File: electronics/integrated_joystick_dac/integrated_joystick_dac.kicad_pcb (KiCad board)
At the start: 2 copper layers, 76.2 x 55.9 mm, 15 parts, among them J1 Power/Signal Out, U1 raspberry_pi_pico, U2 MCP4728

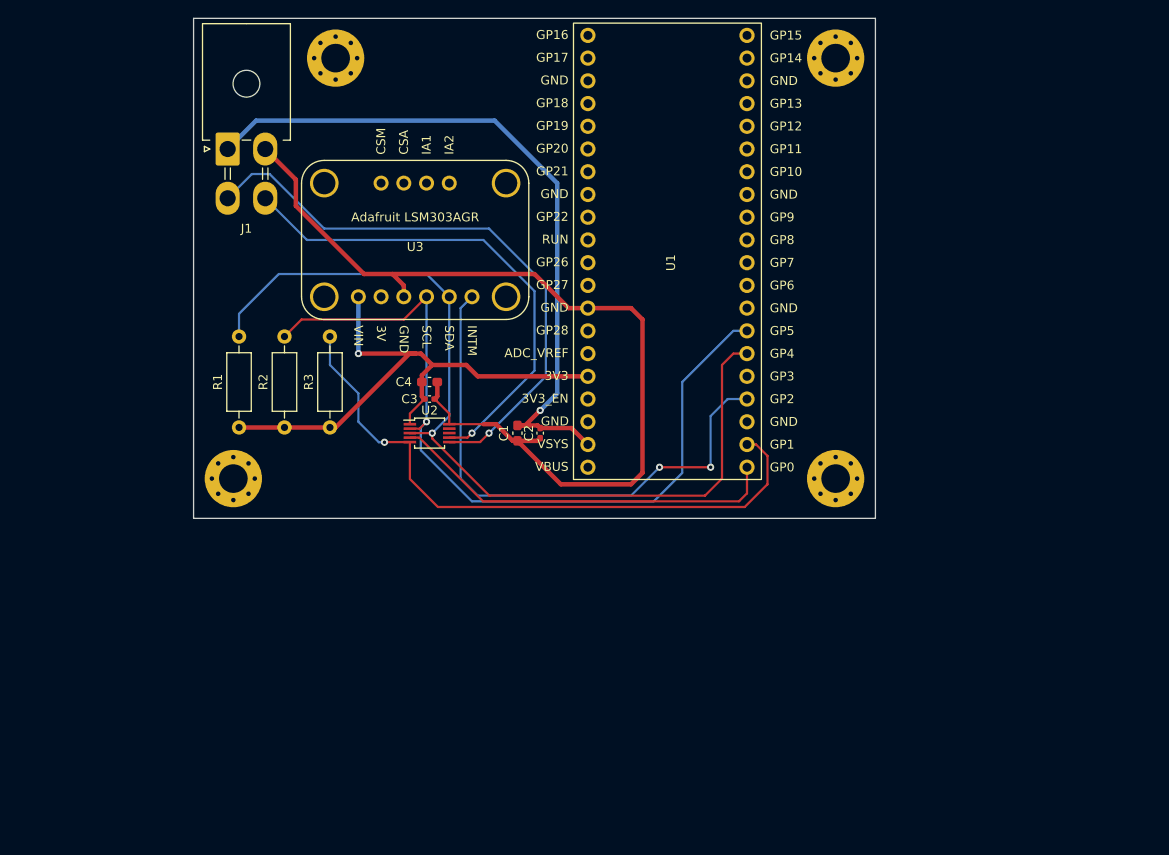
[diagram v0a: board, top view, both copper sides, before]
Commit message: start redoing board since it's too big
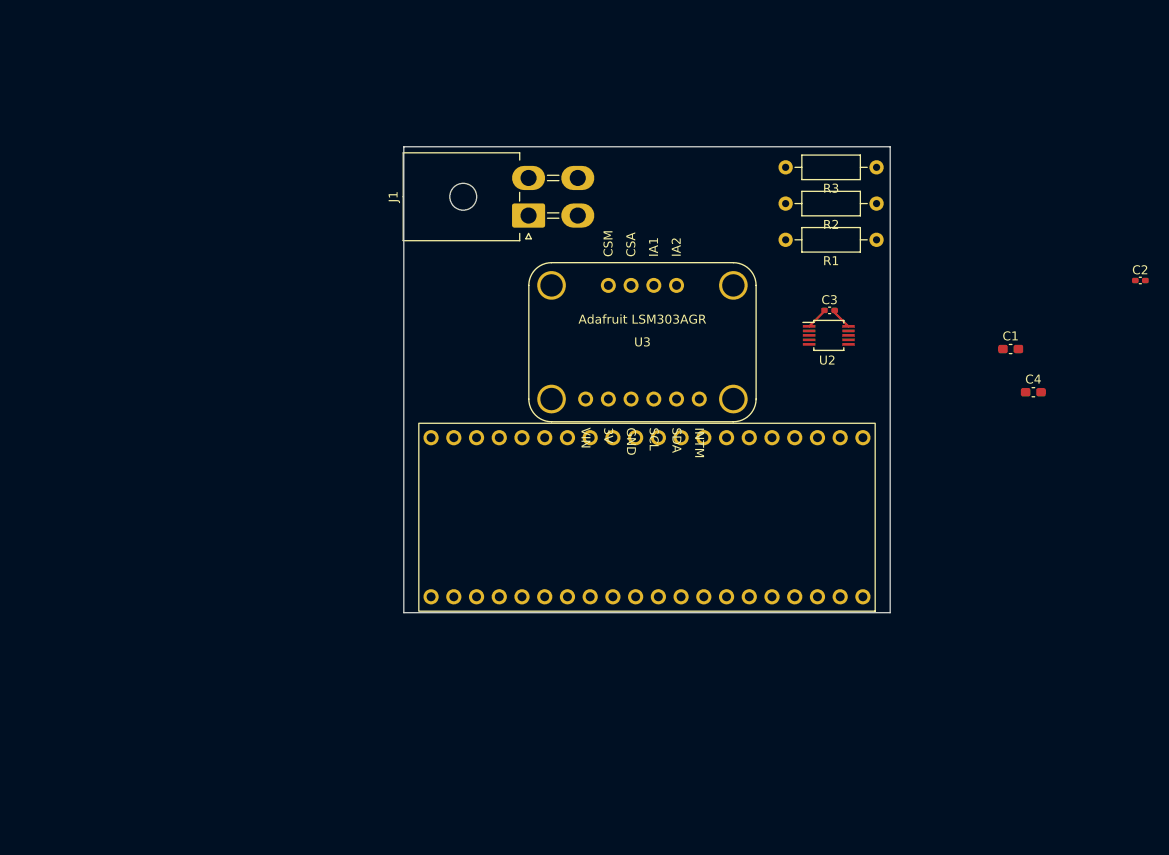
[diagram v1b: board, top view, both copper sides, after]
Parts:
- removed REF** (x4): MountingHole_3.2mm_M3_Pad_Via, MountingHole:MountingHole_3.2mm_M3_Pad_Via
- moved R1 74.3 mm to (206.5, 62.2), turned to 180 degrees
- moved R2 70.7 mm to (206.5, 58.2), turned to 180 degrees
- moved C2 69.2 mm to (236.0, 66.8), turned to 0 degrees
- moved R3 67.7 mm to (206.5, 54.1), turned to 180 degrees
- moved C4 67.5 mm to (224.0, 79.2)
- moved C1 55.9 mm to (221.5, 74.4), turned to 0 degrees
- moved U2 45.9 mm to (201.2, 72.9)
- moved C3 45.8 mm to (201.3, 70.1)
- moved J1 34.4 mm to (167.6, 59.5), turned to 90 degrees
- moved U1 28.2 mm to (182.1, 92.8), turned to 180 degrees
- moved U3 27.4 mm to (180.3, 73.7)
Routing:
- net GND: track 105.0 -> 2.43 mm
- net /SDA: track 99.9 -> 0.00 mm, vias 1 -> 0
- net /SCL: track 90.0 -> 0.00 mm, vias 1 -> 0
- net /+3V3: track 79.2 -> 0.00 mm, vias 1 -> 0
- net /RDY: track 70.0 -> 0.00 mm, vias 1 -> 0
- net /JoystickX: track 65.8 -> 0.00 mm, vias 1 -> 0
- net /+3V3_2: track 64.1 -> 2.51 mm, vias 1 -> 0
- net /INTM: track 61.5 -> 0.00 mm, vias 2 -> 0
- net /JoystickY: track 55.9 -> 0.00 mm, vias 1 -> 0
- net /LDAC: track 43.9 -> 0.00 mm
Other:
- board size 76.2 x 55.9 mm -> 54.4 x 52.1 mm

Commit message: make smaller board...
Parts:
- added REF**: MountingHole_2.7mm_M2.5_ISO7380_Pad, MountingHole:MountingHole_2.7mm_M2.5_ISO7380_Pad, F.Cu at (197.4, 78.5)
- added REF**: MountingHole_2.7mm_M2.5_ISO7380_Pad, MountingHole:MountingHole_2.7mm_M2.5_ISO7380_Pad, F.Cu at (159.3, 77.2)
- added REF**: MountingHole_2.7mm_M2.5_ISO7380_Pad, MountingHole:MountingHole_2.7mm_M2.5_ISO7380_Pad, F.Cu at (191.0, 55.6)
- moved C1 55.6 mm to (166.9, 63.8)
- moved C2 48.0 mm to (200.9, 99.6), turned to 180 degrees
- moved C4 33.5 mm to (197.4, 99.6)
- moved R1 1.62 mm to (206.0, 63.8)
- moved J1 1.30 mm to (168.9, 59.4)
- moved R2 0.92 mm to (206.0, 58.9)
- moved R3 0.51 mm to (206.0, 54.1)
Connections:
- U1 pad 13: unconnected-(U1-GND-Pad13) -> GND
- U1 pad 18: unconnected-(U1-GND-Pad18) -> GND
- U1 pad 23: unconnected-(U1-GND-Pad23) -> GND
- U1 pad 28: unconnected-(U1-GND-Pad28) -> GND
- U1 pad 3: unconnected-(U1-GND-Pad3) -> GND
- U1 pad 38: unconnected-(U1-GND-Pad38) -> GND
- U1 pad 8: unconnected-(U1-GND-Pad8) -> GND
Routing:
- net GND: track 2.43 -> 175.8 mm, vias 0 -> 1
- net /+3V3: track 0.00 -> 97.8 mm
- net /+3V3_2: track 2.51 -> 93.8 mm
- net /SCL: track 0.00 -> 73.3 mm
- net /SDA: track 0.00 -> 55.4 mm, vias 0 -> 1
- net /RDY: track 0.00 -> 47.2 mm
- net /JoystickY: track 0.00 -> 36.8 mm, vias 0 -> 1
- net /JoystickX: track 0.00 -> 34.9 mm, vias 0 -> 1
- net /INTM: track 0.00 -> 15.3 mm
- net /LDAC: track 0.00 -> 14.0 mm
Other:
- board size 54.4 x 52.1 mm -> 53.3 x 52.1 mm
- board text added: "SCTS Engineering Umptysquatch X Joystick DAC Board"

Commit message: move connector back (probably too far)
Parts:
- removed the REF** at (191.0, 55.6)
- moved C1 20.1 mm to (186.9, 63.5)
- moved J1 17.3 mm to (186.2, 59.4)
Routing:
- net /+3V3: track 97.8 -> 114.9 mm
- net /JoystickX: track 34.9 -> 20.2 mm
- net /JoystickY: track 36.8 -> 23.6 mm
- net GND: track 175.8 -> 179.8 mm

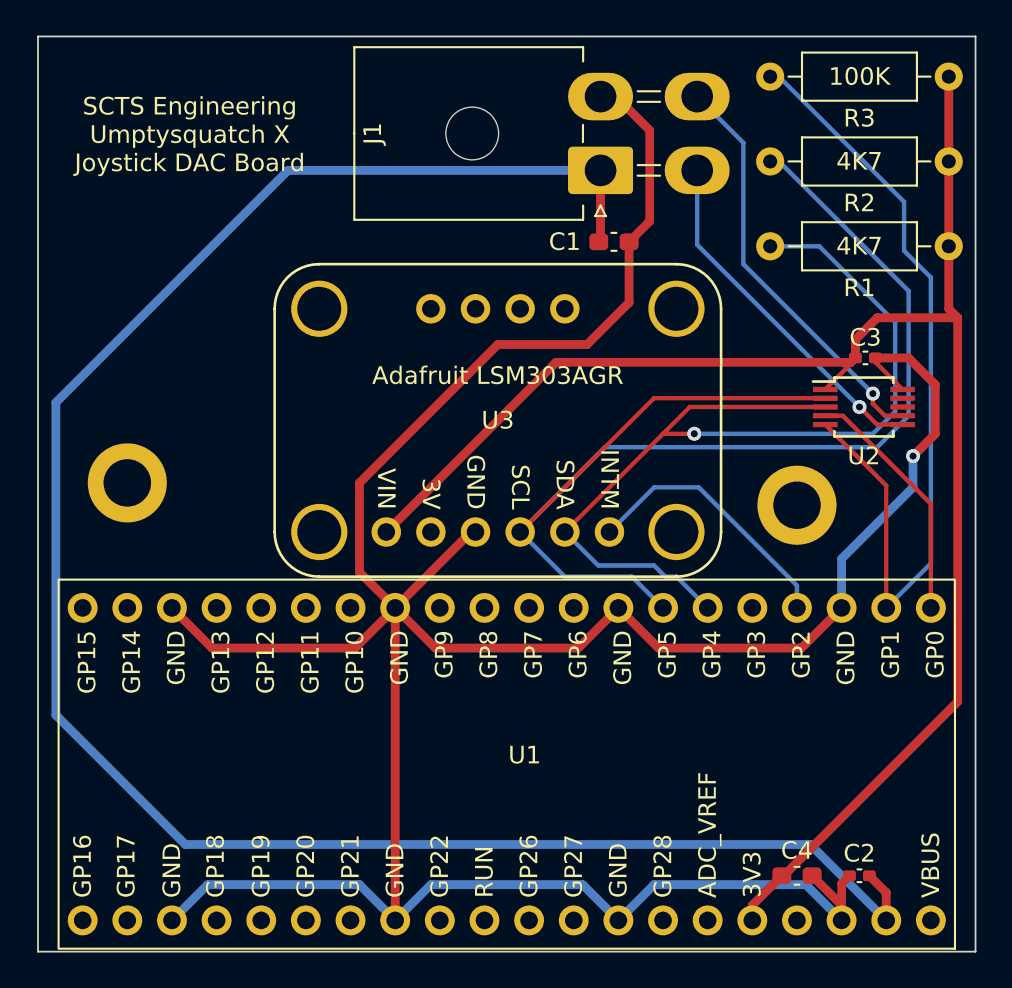
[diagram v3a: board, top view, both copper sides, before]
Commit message: cutout for connector
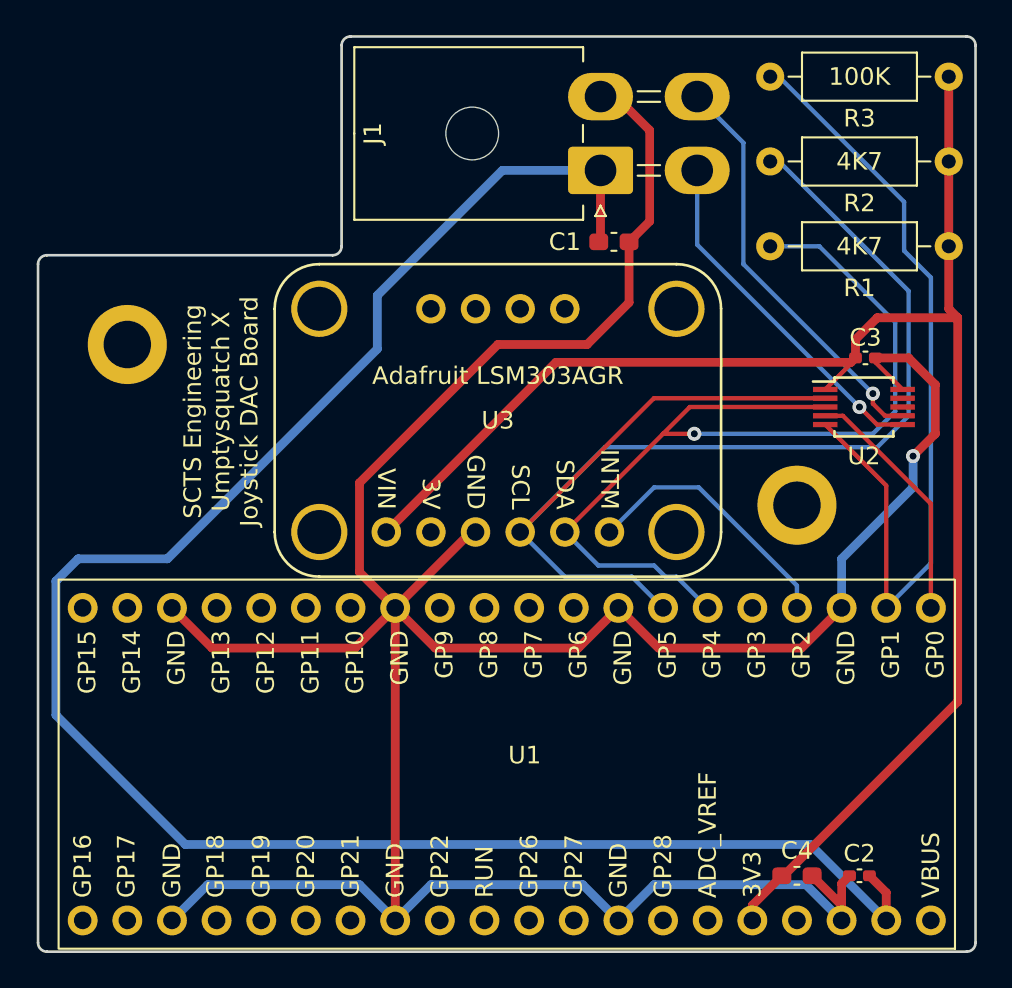
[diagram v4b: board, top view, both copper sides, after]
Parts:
- moved REF** 7.87 mm to (159.3, 69.3)
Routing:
- net /+3V3: track 114.9 -> 110.7 mm
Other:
- outline, holes or cut-outs redrawn
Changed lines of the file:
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@@
   )
   (footprint "MountingHole:MountingHole_2.7mm_M2.5_ISO7380_Pad" locked (layer "F.Cu")
-    (at 159.258 77.216)
+    (at 159.258 69.342)
     (descr "Mounting Hole 2.7mm, M2.5, ISO7380")
     (tags "mounting hole 2.7mm m2.5 iso7380")
@@
   (gr_arc (start 154.94 105.41) (mid 150.449872 103.550128) (end 148.59 99.06)
     (stroke (width 0.15) (type default)) (layer "Dwgs.User"))
-  (gr_rect (start 154.178 51.816) (end 207.518 103.886)
-    (stroke (width 0.1) (type default)) (fill none) (layer "Edge.Cuts"))
-  (gr_text "SCTS Engineering\nUmptysquatch X\nJoystick DAC Board" (at 162.814 57.404) (layer "F.SilkS")
+  (gr_line (start 154.178 103.378) (end 154.178 64.77)
+    (stroke (width 0.15) (type default)) (layer "Edge.Cuts"))
+  (gr_line (start 154.686 103.886) (end 207.01 103.886)
+    (stroke (width 0.15) (type default)) (layer "Edge.Cuts"))
+  (gr_arc (start 171.45 63.754) (mid 171.301211 64.113211) (end 170.942 64.262)
+    (stroke (width 0.15) (type default)) (layer "Edge.Cuts"))
+  (gr_arc (start 207.01 51.816) (mid 207.369211 51.964789) (end 207.518 52.324)
+    (stroke (width 0.15) (type default)) (layer "Edge.Cuts"))
+  (gr_arc (start 207.518 103.378) (mid 207.369211 103.737211) (end 207.01 103.886)
+    (stroke (width 0.15) (type default)) (layer "Edge.Cuts"))
+  (gr_arc (start 154.686 103.886) (mid 154.326789 103.737211) (end 154.178 103.378)
+    (stroke (width 0.15) (type default)) (layer "Edge.Cuts"))
+  (gr_line (start 207.01 51.816) (end 171.958 51.816)
+    (stroke (width 0.15) (type default)) (layer "Edge.Cuts"))
+  (gr_line (start 154.686 64.262) (end 170.942 64.262)
+    (stroke (width 0.15) (type default)) (layer "Edge.Cuts"))
+  (gr_arc (start 154.178 64.77) (mid 154.326789 64.410789) (end 154.686 64.262)
+    (stroke (width 0.15) (type default)) (layer "Edge.Cuts"))
+  (gr_line (start 171.45 52.324) (end 171.45 63.754)
+    (stroke (width 0.15) (type default)) (layer "Edge.Cuts"))
+  (gr_arc (start 171.45 52.324) (mid 171.598789 51.964789) (end 171.958 51.816)
+    (stroke (width 0.15) (type default)) (layer "Edge.Cuts"))
+  (gr_line (start 207.518 103.378) (end 207.518 52.324)
+    (stroke (width 0.15) (type default)) (layer "Edge.Cuts"))
+  (gr_text "SCTS Engineering\nUmptysquatch X\nJoystick DAC Board" (at 164.592 73.152 90) (layer "F.SilkS")
     (effects (font (size 1 1) (thickness 0.15)))
   )
@@
   (segment (start 202.438 100.5245) (end 202.438 102.108) (width 0.5) (layer "F.Cu") (net 32))
   (segment (start 201.4815 99.568) (end 202.438 100.5245) (width 0.5) (layer "F.Cu") (net 32))
-  (segment (start 168.402 59.436) (end 155.194 72.644) (width 0.5) (layer "B.Cu") (net 32))
+  (segment (start 198.12 97.79) (end 202.438 102.108) (width 0.5) (layer "B.Cu") (net 32))
+  (segment (start 173.482 66.548) (end 173.482 69.596) (width 0.5) (layer "B.Cu") (net 32))
+  (segment (start 156.464 81.534) (end 155.194 82.804) (width 0.5) (layer "B.Cu") (net 32))
+  (segment (start 162.56 97.79) (end 198.12 97.79) (width 0.5) (layer "B.Cu") (net 32))
   (segment (start 155.194 90.424) (end 162.56 97.79) (width 0.5) (layer "B.Cu") (net 32))
-  (segment (start 162.56 97.79) (end 198.12 97.79) (width 0.5) (layer "B.Cu") (net 32))
-  (segment (start 155.194 72.644) (end 155.194 90.424) (width 0.5) (layer "B.Cu") (net 32))
-  (segment (start 186.182 59.436) (end 168.402 59.436) (width 0.5) (layer "B.Cu") (net 32))
-  (segment (start 198.12 97.79) (end 202.438 102.108) (width 0.5) (layer "B.Cu") (net 32))
+  (segment (start 161.544 81.534) (end 156.464 81.534) (width 0.5) (layer "B.Cu") (net 32))
+  (segment (start 155.194 82.804) (end 155.194 90.424) (width 0.5) (layer "B.Cu") (net 32))
+  (segment (start 180.594 59.436) (end 173.482 66.548) (width 0.5) (layer "B.Cu") (net 32))
+  (segment (start 173.482 69.596) (end 161.544 81.534) (width 0.5) (layer "B.Cu") (net 32))
+  (segment (start 186.182 59.436) (end 180.594 59.436) (width 0.5) (layer "B.Cu") (net 32))
   (segment (start 201.914 73.898) (end 200.914 72.898) (width 0.25) (layer "F.Cu") (net 34))
   (segment (start 203.368 73.898) (end 201.914 73.898) (width 0.25) (layer "F.Cu") (net 34))

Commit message: modify pcb and schematic sheets for export for design report
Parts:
- moved C4 50.2 mm to (153.8, 124.6)
- moved R2 50.2 mm to (162.4, 83.9)
- moved REF** 50.2 mm to (115.7, 94.4)
- moved U1 50.2 mm to (138.5, 117.9)
- moved U2 50.2 mm to (157.6, 97.9)
- moved U3 50.2 mm to (136.8, 98.7)
- moved R1 50.2 mm to (162.4, 88.8)
- moved R3 50.2 mm to (162.4, 79.1)
- moved REF** 50.2 mm to (153.8, 103.5)
- moved C1 50.2 mm to (143.4, 88.5)
- moved C2 50.2 mm to (157.4, 124.6)
- moved C3 50.2 mm to (157.7, 95.1)
- moved J1 50.2 mm to (142.6, 84.5)
